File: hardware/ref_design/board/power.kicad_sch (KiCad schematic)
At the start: 19 parts, among them Q1 2N7002, U3 ME6211C33M5G

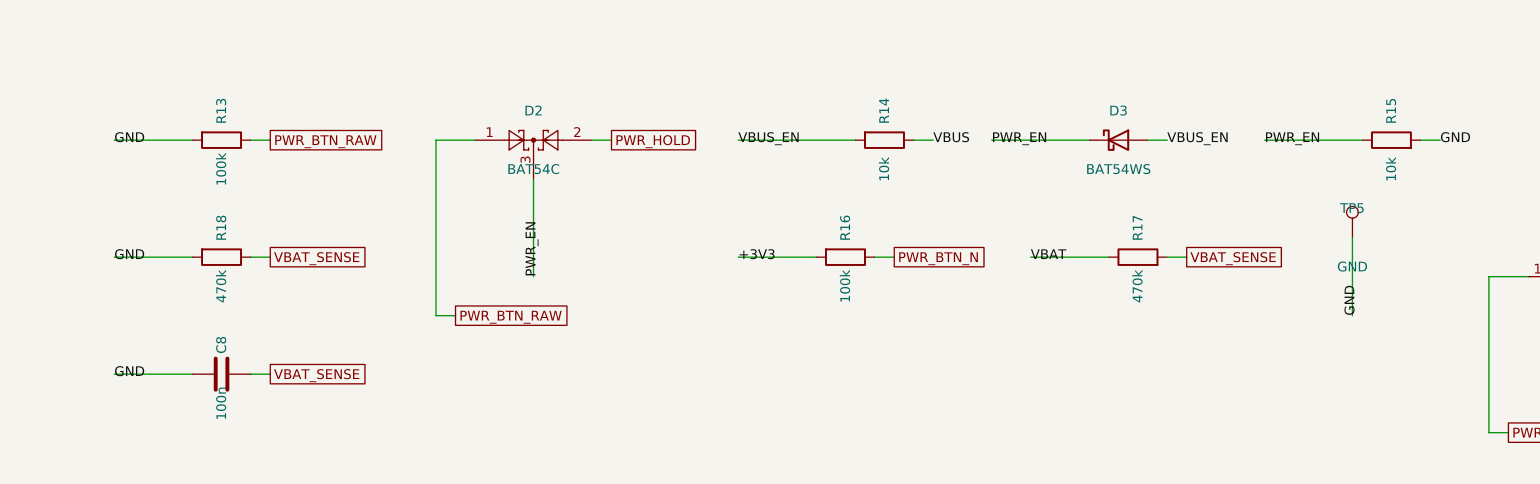
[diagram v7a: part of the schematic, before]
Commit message: Reference design: audit round 2 fixes (VBUS bleeder, window, fit check)
- R15 back to 100k and a 10k VBUS bleeder (R38) instead: the 10k R15 cut the
  Y contact's pill-resistance margin for Q1 about five times. The bleeder
  needs about 140 uA of D5 leakage before CE reaches 1.0 V; 0.5 mA on USB.
  R38 sits beside R14 (next to C1 it blocked seat 1's A route).
- Lid window margin 0.5 -> 0.8 mm: covers the panel's +-0.4 float in its
  frame and its +-0.3 active-area tolerance. Frame wall and depth named.
- check_fit.py knows the lid's panel frame: parts under its band are held
  to its lower limit (3.6 mm).
- route.py: the final cleanup also drops a pour's via that joins nothing
  (a stitching via left in a pocket the pours never reached).

Checks: netlist PASS (123 parts), ERC 0, DRC 0 errors / 0 unconnected /
0 parity (2 cosmetic silk warnings), fit PASS on 92 parts.

Co-Authored-By: Claude Opus 5.5 <noreply@anthropic.com>
Claude-Session: https://claude.ai/code/session_01KGgEu3CbFtCsvHRQgAFiCN
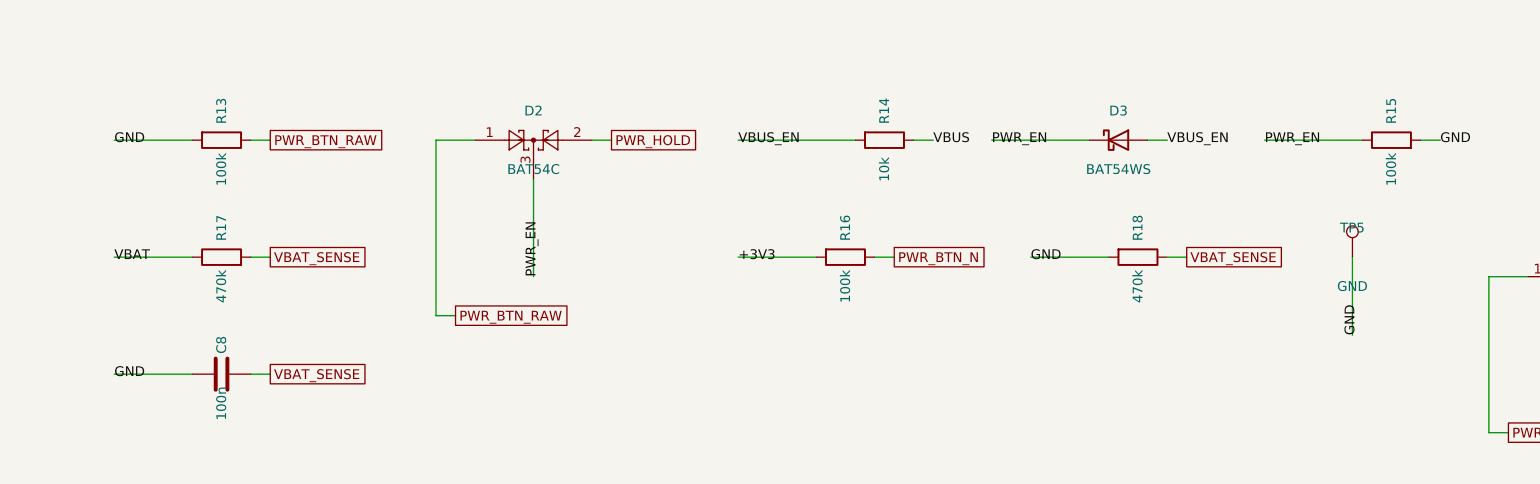
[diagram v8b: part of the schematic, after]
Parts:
- R15: value 10k -> 100k; LCSC C25744 -> C25741; MPN 0402WGF1002TCE -> 0402WGF1003TCE
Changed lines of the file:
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@@
+  (wire
+    (pts
+      (xy 26.67 106.68)
+      (xy 16.51 106.68))
+)
+  (wire
+    (pts
+      (xy 34.29 106.68)
+      (xy 36.83 106.68))
+)
+  (wire
+    (pts
+      (xy 153.67 106.68)
+      (xy 156.21 106.68))
+)
   (wire
     (pts
@@
   (wire
     (pts
-      (xy 153.67 106.68)
-      (xy 156.21 106.68))
-)
-  (wire
-    (pts
-      (xy 34.29 106.68)
-      (xy 36.83 106.68))
-)
-  (wire
-    (pts
-      (xy 26.67 106.68)
-      (xy 16.51 106.68))
-)
-  (wire
-    (pts
       (xy 34.29 121.92)
       (xy 36.83 121.92))
@@
   (wire
     (pts
-      (xy 177.8 104.14)
-      (xy 177.8 114.3))
+      (xy 177.8 106.68)
+      (xy 177.8 116.84))
 )
   (wire
@@
 )
   (label "VBAT"
+    (at 16.51 106.68 0)
+)
+  (label "GND"
     (at 135.89 106.68 0)
-)
-  (label "GND"
-    (at 16.51 106.68 0)
 )
   (label "GND"
@@
 )
   (label "GND"
-    (at 177.8 114.3 90)
+    (at 177.8 116.84 90)
 )
   (label "GND"
@@
   (global_label "VBAT_SENSE"
     (shape passive)
-    (at 156.21 106.68 0)
+    (at 36.83 106.68 0)
 )
   (global_label "VBAT_SENSE"
     (shape passive)
-    (at 36.83 106.68 0)
+    (at 156.21 106.68 0)
 )
   (global_label "VBAT_SENSE"
@@
         (font
           (size 1.27 1.27))))
-    (property "Value" "10k"
+    (property "Value" "100k"
       (at 182.88 95.25 0)
       (effects
@@
           (size 1.27 1.27))
         (hide yes)))
-    (property "LCSC" "C25744"
-      (at 0 0 0)
-      (effects
-        (font
-          (size 1.27 1.27))
-        (hide yes)))
-    (property "MPN" "0402WGF1002TCE"
+    (property "LCSC" "C25741"
+      (at 0 0 0)
+      (effects
+        (font
+          (size 1.27 1.27))
+        (hide yes)))
+    (property "MPN" "0402WGF1003TCE"
       (at 0 0 0)
       (effects
@@
   (symbol
     (lib_id "Device:R")
-    (at 149.86 106.68 90)
+    (at 30.48 106.68 90)
     (unit 1)
     (in_bom yes)
@@
     (dnp no)
     (property "Reference" "R17"
+      (at 30.48 102.87 0)
+      (effects
+        (font
+          (size 1.27 1.27))))
+    (property "Value" "470k"
+      (at 30.48 110.49 0)
+      (effects
+        (font
+          (size 1.27 1.27))))
+    (property "Footprint" "Resistor_SMD:R_0402_1005Metric"
+      (at 30.48 106.68 0)
+      (effects
+        (font
+          (size 1.27 1.27))
+        (hide yes)))
+    (property "Datasheet" ""
+      (at 30.48 106.68 0)
+      (effects
+        (font
+          (size 1.27 1.27))
+        (hide yes)))
+    (property "LCSC" "C25790"
+      (at 0 0 0)
+      (effects
+        (font
+          (size 1.27 1.27))
+        (hide yes)))
+    (property "MPN" "0402WGF4703TCE"
+      (at 0 0 0)
+      (effects
+        (font
+          (size 1.27 1.27))
+        (hide yes)))
+    (property "Manufacturer" "UNI-ROYAL"
+      (at 0 0 0)
+      (effects
+        (font
+          (size 1.27 1.27))
+        (hide yes)))
+    (instances
+      (project ""
+        (path "/"
+          (reference "R17")
+          (unit 1)))))
+  (symbol
+    (lib_id "Device:R")
+    (at 149.86 106.68 270)
+    (unit 1)
+    (in_bom yes)
+    (on_board yes)
+    (dnp no)
+    (property "Reference" "R18"
       (at 149.86 102.87 0)
       (effects
@@
       (project ""
         (path "/"
-          (reference "R17")
-          (unit 1)))))
-  (symbol
-    (lib_id "Device:R")
-    (at 30.48 106.68 270)
-    (unit 1)
-    (in_bom yes)
-    (on_board yes)
-    (dnp no)
-    (property "Reference" "R18"
-      (at 30.48 102.87 0)
-      (effects
-        (font
-          (size 1.27 1.27))))
-    (property "Value" "470k"
-      (at 30.48 110.49 0)
-      (effects
-        (font
-          (size 1.27 1.27))))
-    (property "Footprint" "Resistor_SMD:R_0402_1005Metric"
-      (at 30.48 106.68 0)
-      (effects
-        (font
-          (size 1.27 1.27))
-        (hide yes)))
-    (property "Datasheet" ""
-      (at 30.48 106.68 0)
-      (effects
-        (font
-          (size 1.27 1.27))
-        (hide yes)))
-    (property "LCSC" "C25790"
-      (at 0 0 0)
-      (effects
-        (font
-          (size 1.27 1.27))
-        (hide yes)))
-    (property "MPN" "0402WGF4703TCE"
-      (at 0 0 0)
-      (effects
-        (font
-          (size 1.27 1.27))
-        (hide yes)))
-    (property "Manufacturer" "UNI-ROYAL"
-      (at 0 0 0)
-      (effects
-        (font
-          (size 1.27 1.27))
-        (hide yes)))
-    (instances
-      (project ""
-        (path "/"
           (reference "R18")
           (unit 1)))))
@@
   (symbol
     (lib_id "Connector:TestPoint")
-    (at 177.8 104.14 0)
+    (at 177.8 106.68 0)
     (unit 1)
     (in_bom yes)
@@
     (dnp no)
     (property "Reference" "TP5"
-      (at 177.8 100.33 0)
+      (at 177.8 102.87 0)
       (effects
         (font
           (size 1.27 1.27))))
     (property "Value" "GND"
-      (at 177.8 107.95 0)
+      (at 177.8 110.49 0)
       (effects
         (font
           (size 1.27 1.27))))
     (property "Footprint" "TestPoint:TestPoint_Pad_D1.0mm"
-      (at 177.8 104.14 0)
-      (effects
-        (font
-          (size 1.27 1.27))
-        (hide yes)))
-    (property "Datasheet" ""
-      (at 177.8 104.14 0)
-      (effects
-        (font
+      (at 177.8 106.68 0)
+      (effects
+        (font
+          (size 1.27 1.27))
+        (hide yes)))
+    (property "Datasheet" ""
+      (at 177.8 106.68 0)
+      (effects
+        (font
